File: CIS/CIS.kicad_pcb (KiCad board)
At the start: 6 copper layers, 125 x 32.5 mm, 187 parts, among them J1 Conn_01x12, J2 RJ45_Abracon_ARJP11A-MASA-B-A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, J3 SJ1-3533NG, J4 DEBUG TAG, K1 K_9999, P3 K_0023, Q1 Q_0002, Q2 Q_0002, Q3 Q_0002, SW1 SW_0003, SW2 SW_0003, SW3 SW_0003, SW4 SW_0003, SW5 SW_0003, U1 U_0076, U14 U_0101, U16 U_0049, U17 U_0049, U2 STM32H745IIKx, U3 U_0103, U4 U_1001, U5 U_0081, U6 U_0097, U7 PCM5102, U8 ICM-20602

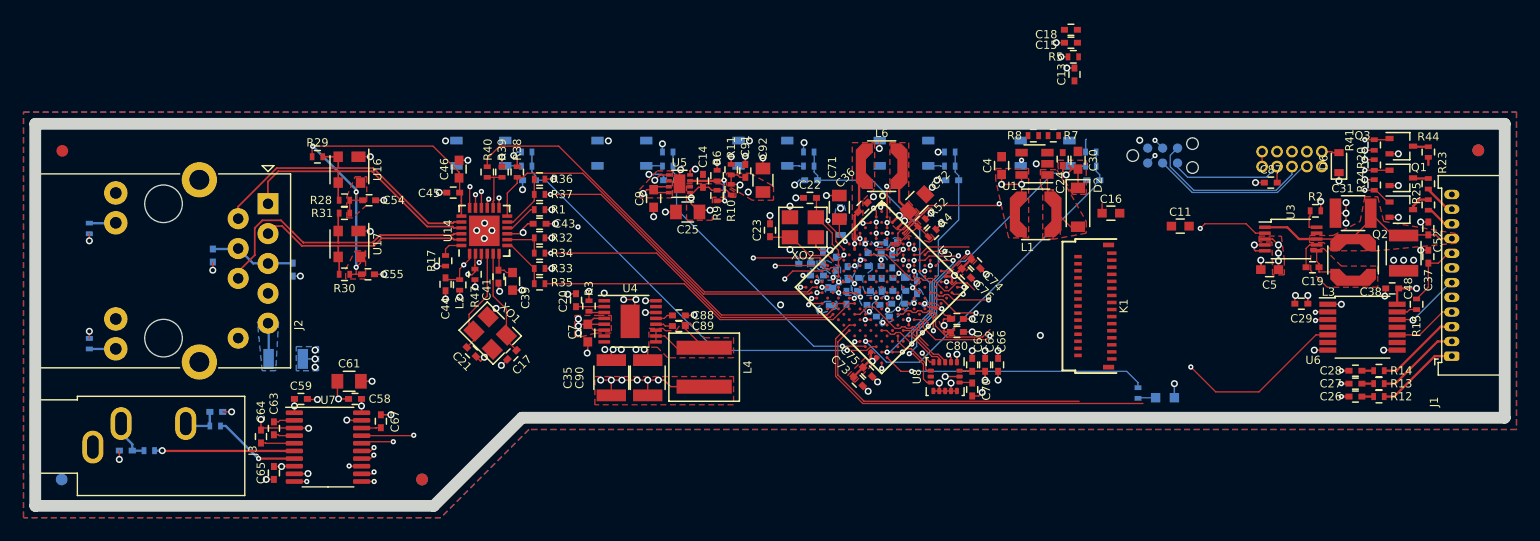
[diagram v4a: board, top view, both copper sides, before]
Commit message: Update oled connector / complete 3D missing part
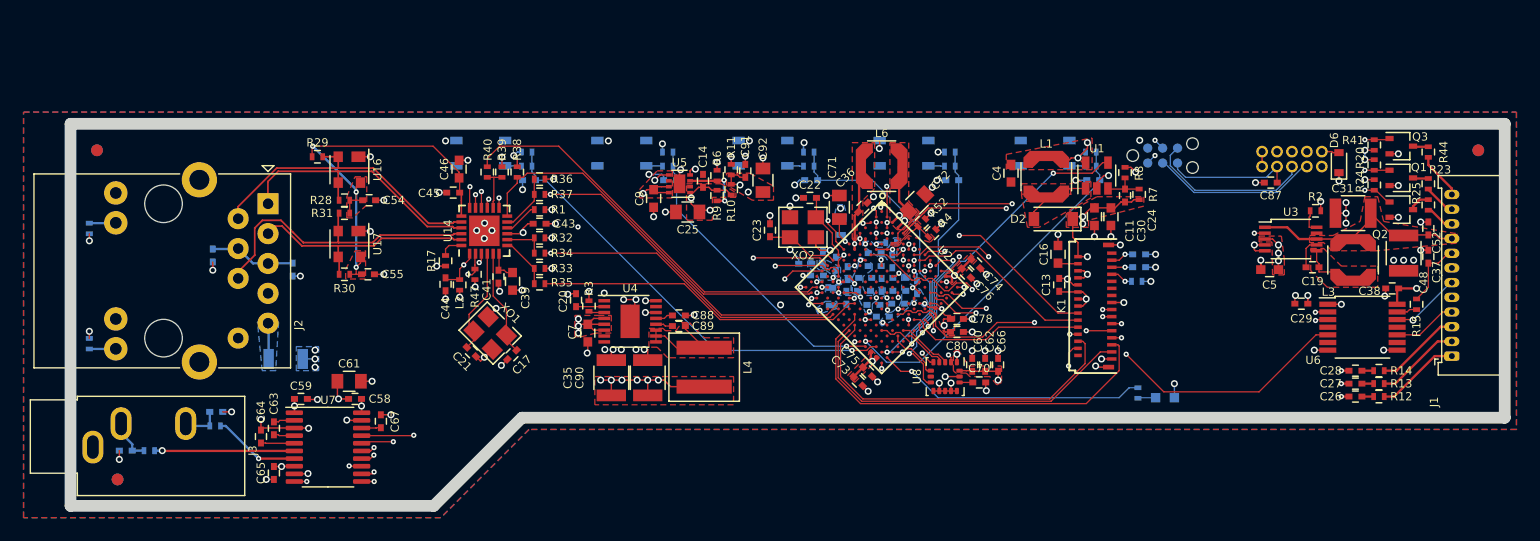
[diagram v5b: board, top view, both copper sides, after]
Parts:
- removed REF4: CircleWhite1mm, DVB_Fiducials:REF_1mm
- added G***: LOGO, DVB_Mechanicals:RESO-NANCE_SSS_LOGO, B.Cu at (50.8, 74.9)
- added G***: LOGO, DVB_Mechanicals:RESO-NANCE_SSS-2_LOGO, B.Cu at (150.2, 84.7)
- added REF12: CircleWhite1mm, DVB_Fiducials:REF_1mm, B.Cu at (46.4, 74.8)
- C15, C18, R5: moved to B.Cu
- moved REF2 25.9 mm to (48.1, 102.8)
- moved C15 20.0 mm to (135.0, 84.7), turned to 0 degrees
- moved C18 20.0 mm to (135.0, 83.6), turned to 0 degrees
- moved R5 19.8 mm to (134.8, 85.9), turned to 180 degrees
- moved C13 17.9 mm to (128.2, 86.2)
- moved R7 8.85 mm to (135.0, 78.5), turned to 90 degrees
- moved R8 8.41 mm to (133.8, 76.7), turned to 90 degrees
- moved C11 7.34 mm to (131.2, 80.4), turned to 270 degrees
- moved C24 6.14 mm to (133.8, 78.6)
- moved C16 5.70 mm to (128.1, 83.6), turned to 90 degrees
- moved C30 5.56 mm to (132.6, 80.4), turned to 270 degrees
- moved U1 5.39 mm to (131.4, 76.9), turned to 90 degrees
- moved REF11 4.75 mm to (48.1, 102.8)
- moved L1 3.32 mm to (127.1, 77.0), turned to 270 degrees
- moved REF1 2.95 mm to (46.4, 74.8)
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- renumbered REF2 to REF1, REF4 to REF11, REF3 to REF13, REF1 to REF3
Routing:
- net /FMC_D5: track 8.34 -> 35.1 mm
- net /DEBUG_RX: track 28.8 -> 51.8 mm
- net /FMC_NEx: track 4.95 -> 19.3 mm, vias 0 -> 2
- net /FMC_Ax: track 10.9 -> 23.5 mm, vias 0 -> 2
- net /FMC_D1: track 9.95 -> 20.8 mm, vias 0 -> 2
- net GND: track 111.1 -> 121.2 mm, vias 133 -> 140
- net /FMC_D2: track 25.3 -> 15.7 mm, vias 1 -> 2
- net /DEBUG_TX: track 44.6 -> 53.4 mm, vias 0 -> 1
- net /FMC_NWE: track 24.7 -> 16.3 mm, vias 1 -> 0
- net /FMC_D0: track 23.0 -> 15.3 mm, vias 1 -> 0
- net /OLED_RESET: track 30.7 -> 23.4 mm, vias 1 -> 2
- net /FMC_D6: track 28.4 -> 21.6 mm, vias 1 -> 2
- net /SWD-IO: track 31.5 -> 37.9 mm, vias 3 -> 2
- net +3.3V: track 66.0 -> 71.3 mm, vias 49 -> 50
- net /12V_EN: track 19.8 -> 24.5 mm, vias 1 -> 2
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- added copper zone on POWER.Cu, net +12V
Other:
- board size 125 x 32.5 mm -> 122 x 32.5 mm

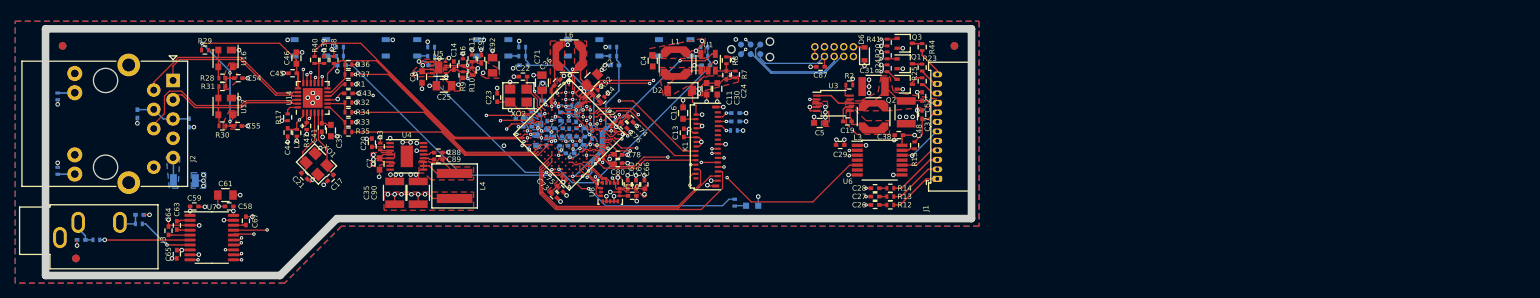
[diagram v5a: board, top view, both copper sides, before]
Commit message: Incert CIS connector
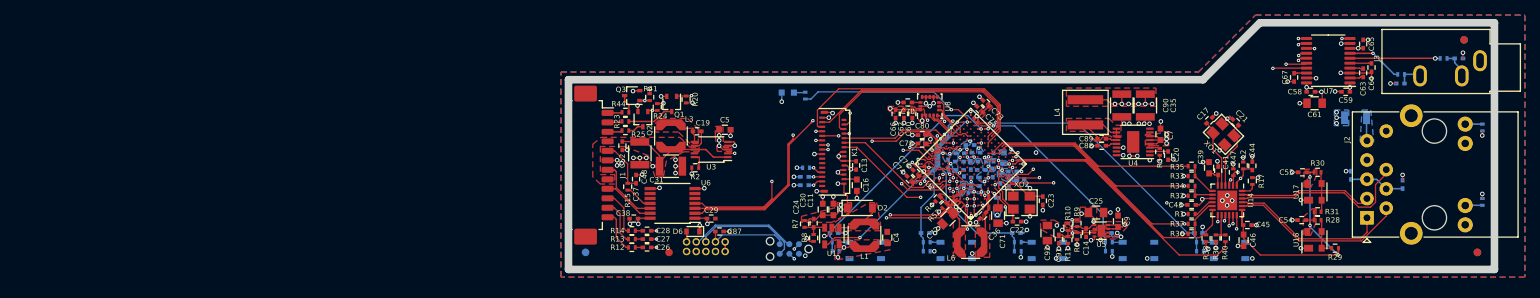
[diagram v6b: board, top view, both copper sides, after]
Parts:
- J1: value Conn_01x12 -> K_9998; footprint DVB_Connectors:Molex_PicoBlade_53048-1210_1x12_P1.25mm_Horizontal -> DVB_Connectors:Molex_PicoBlade_53261-1271_1x12-1MP_P1.25mm_Horizontal
- moved J3 188.5 mm to (233.1, 76.7), turned to 270 degrees
- moved REF1 188.4 mm to (232.8, 102.0), turned to 90 degrees
- moved REF12 188.4 mm to (232.8, 102.0), turned to 180 degrees
- moved R48 188.2 mm to (233.4, 95.3), turned to 90 degrees
- moved R49 187.8 mm to (233.4, 85.5), turned to 270 degrees
- moved REF11 185.2 mm to (231.0, 74.0), turned to 180 degrees
- moved REF2 185.2 mm to (231.0, 74.0), turned to 90 degrees
- moved C69 183.1 mm to (230.3, 76.4), turned to 0 degrees
- moved R50 179.1 mm to (228.3, 76.4), turned to 0 degrees
- moved G*** 172.8 mm to (223.6, 74.1), turned to 180 degrees
- moved R51 167.5 mm to (222.7, 78.5), turned to 180 degrees
- moved C68 167.0 mm to (222.6, 79.7), turned to 180 degrees
- moved C49 167.0 mm to (222.9, 93.0), turned to 90 degrees
- moved C64 160.0 mm to (218.8, 77.6), turned to 90 degrees
- moved C65 158.7 mm to (217.7, 74.5), turned to 90 degrees
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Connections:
- J1 pad 1: Net-(J1-Pad1) -> /CIS_VLED_B
- J1 pad 10: /CIS_VLED_G -> Net-(J1-Pad10)
- J1 pad 11: /CIS_VLED_R -> Net-(J1-Pad11)
- J1 pad 12: /CIS_VLED_B -> Net-(J1-Pad12)
- J1 pad 2: Net-(J1-Pad2) -> /CIS_VLED_R
- J1 pad 3: Net-(J1-Pad3) -> /CIS_VLED_G
- J1 pad 4: /CIS_RS_TTL -> +5V
- J1 pad 5: +5V -> Net-(C37-Pad2)
- J1 pad 6: /CIS_SP_TTL -> GND
- J1 pad 7: GND -> /CIS_SP_TTL
- J1 pad 8: Net-(C37-Pad2) -> +5V
- J1 pad 9: +5V -> /CIS_RS_TTL
- K1 pad 30: (no net) -> Net-(K1-Pad30)
- K1 pad 9: (no net) -> Net-(K1-Pad9)
- P3 pad 7: (no net) -> Net-(P3-Pad7)
- R12 pad 2: Net-(J1-Pad1) -> Net-(J1-Pad12)
- R13 pad 2: Net-(J1-Pad2) -> Net-(J1-Pad11)
- R14 pad 2: Net-(J1-Pad3) -> Net-(J1-Pad10)
- SW1 pad 1: (no net) -> Net-(SW1-Pad1)
- SW1 pad 4: (no net) -> Net-(SW1-Pad4)
- SW2 pad 1: (no net) -> Net-(SW2-Pad1)
- SW2 pad 4: (no net) -> Net-(SW2-Pad4)
- SW3 pad 1: (no net) -> Net-(SW3-Pad1)
- SW3 pad 4: (no net) -> Net-(SW3-Pad4)
- SW4 pad 1: (no net) -> Net-(SW4-Pad1)
- SW4 pad 4: (no net) -> Net-(SW4-Pad4)
- SW5 pad 1: (no net) -> Net-(SW5-Pad1)
- SW5 pad 4: (no net) -> Net-(SW5-Pad4)
- U2 pad A6: (no net) -> Net-(U2-PadA6)
- U2 pad A8: (no net) -> Net-(U2-PadA8)
- U2 pad B10: (no net) -> Net-(U2-PadB10)
- U2 pad B11: (no net) -> Net-(U2-PadB11)
- U2 pad B12: (no net) -> Net-(U2-PadB12)
- U2 pad B14: (no net) -> Net-(U2-PadB14)
- U2 pad B2: (no net) -> Net-(U2-PadB2)
- U2 pad B4: (no net) -> Net-(U2-PadB4)
- U2 pad B6: (no net) -> Net-(U2-PadB6)
- U2 pad C11: (no net) -> Net-(U2-PadC11)
- U2 pad C12: (no net) -> Net-(U2-PadC12)
- U2 pad C13: (no net) -> Net-(U2-PadC13)
- U2 pad C14: (no net) -> Net-(U2-PadC14)
- U2 pad C15: (no net) -> Net-(U2-PadC15)
- U2 pad C4: (no net) -> Net-(U2-PadC4)
- U2 pad C6: (no net) -> Net-(U2-PadC6)
- U2 pad C8: (no net) -> Net-(U2-PadC8)
- U2 pad D1: (no net) -> Net-(U2-PadD1)
- U2 pad D12: (no net) -> Net-(U2-PadD12)
- U2 pad D15: (no net) -> Net-(U2-PadD15)
- U2 pad D2: (no net) -> Net-(U2-PadD2)
- U2 pad D7: (no net) -> Net-(U2-PadD7)
- U2 pad D8: (no net) -> Net-(U2-PadD8)
- U2 pad E13: (no net) -> Net-(U2-PadE13)
- U2 pad E14: /CIS_LED_R -> /CIS_LED_B
- U2 pad E3: (no net) -> Net-(U2-PadE3)
- U2 pad F14: (no net) -> Net-(U2-PadF14)
- U2 pad F3: (no net) -> Net-(U2-PadF3)
- U2 pad G12: (no net) -> Net-(U2-PadG12)
- U2 pad G13: (no net) -> Net-(U2-PadG13)
- U2 pad G14: (no net) -> Net-(U2-PadG14)
- U2 pad G3: (no net) -> Net-(U2-PadG3)
- U2 pad H13: (no net) -> Net-(U2-PadH13)
- U2 pad H15: /CIS_LED_G -> /CIS_LED_R
- U2 pad H2: (no net) -> Net-(U2-PadH2)
- U2 pad H3: (no net) -> Net-(U2-PadH3)
- U2 pad H4: (no net) -> Net-(U2-PadH4)
- U2 pad J13: (no net) -> Net-(U2-PadJ13)
- U2 pad J15: (no net) -> Net-(U2-PadJ15)
- U2 pad J2: (no net) -> Net-(U2-PadJ2)
- U2 pad J3: (no net) -> Net-(U2-PadJ3)
- U2 pad J4: (no net) -> Net-(U2-PadJ4)
- U2 pad K13: (no net) -> Net-(U2-PadK13)
- U2 pad K3: (no net) -> Net-(U2-PadK3)
- U2 pad L13: (no net) -> Net-(U2-PadL13)
- U2 pad L15: (no net) -> Net-(U2-PadL15)
- U2 pad L2: (no net) -> Net-(U2-PadL2)
- U2 pad M11: (no net) -> Net-(U2-PadM11)
- U2 pad M13: (no net) -> Net-(U2-PadM13)
- U2 pad M14: (no net) -> Net-(U2-PadM14)
- U2 pad M15: (no net) -> Net-(U2-PadM15)
- U2 pad M2: (no net) -> Net-(U2-PadM2)
- U2 pad M8: (no net) -> Net-(U2-PadM8)
- U2 pad N1: (no net) -> Net-(U2-PadN1)
- U2 pad N10: (no net) -> Net-(U2-PadN10)
- U2 pad N11: (no net) -> Net-(U2-PadN11)
- U2 pad N12: (no net) -> Net-(U2-PadN12)
- U2 pad N13: (no net) -> Net-(U2-PadN13)
- U2 pad N14: (no net) -> Net-(U2-PadN14)
- U2 pad N15: /CIS_LED_B -> /CIS_LED_G
- U2 pad N4: (no net) -> Net-(U2-PadN4)
- U2 pad N5: (no net) -> Net-(U2-PadN5)
- U2 pad N7: (no net) -> Net-(U2-PadN7)
- U2 pad N9: (no net) -> Net-(U2-PadN9)
- U2 pad P1: (no net) -> Net-(U2-PadP1)
- U2 pad P10: (no net) -> Net-(U2-PadP10)
- U2 pad P11: (no net) -> Net-(U2-PadP11)
- U2 pad P4: (no net) -> Net-(U2-PadP4)
- U2 pad P5: (no net) -> Net-(U2-PadP5)
- U2 pad P6: (no net) -> Net-(U2-PadP6)
- U2 pad P7: (no net) -> Net-(U2-PadP7)
- U2 pad P8: (no net) -> Net-(U2-PadP8)
- U2 pad R10: (no net) -> Net-(U2-PadR10)
- U2 pad R5: (no net) -> Net-(U2-PadR5)
- U2 pad R7: (no net) -> Net-(U2-PadR7)
- U2 pad R8: (no net) -> Net-(U2-PadR8)
- U3 pad 9: (no net) -> Net-(U3-Pad9)
- U4 pad 15: (no net) -> Net-(U4-Pad15)
- U4 pad 7: (no net) -> Net-(U4-Pad7)
- U5 pad 6: (no net) -> Net-(U5-Pad6)
- U6 pad 10: /CIS_RS_TTL -> Net-(U6-Pad10)
- U6 pad 11: (no net) -> /CIS_CP_TTL
- U6 pad 13: /CIS_CP_TTL -> /CIS_RS_TTL
- U6 pad 2: /CIS_CP -> /CIS_RS
- U6 pad 4: (no net) -> /CIS_CP
- U6 pad 5: /CIS_RS -> Net-(U6-Pad5)
- U6 pad 6: (no net) -> Net-(U6-Pad6)
- U6 pad 9: (no net) -> Net-(U6-Pad9)
- U8 pad 7: (no net) -> Net-(U8-Pad7)
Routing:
- net /CIS_ADC_3: track 50.1 -> 68.1 mm
- net /CIS_ADC_2: track 51.8 -> 67.6 mm
- net /CIS_ADC_1: track 54.5 -> 68.2 mm
- net Net-(J1-Pad3): track 7.30 -> 0.00 mm
- net Net-(J1-Pad2): track 7.24 -> 0.00 mm
- net Net-(J1-Pad1): track 7.18 -> 0.00 mm
- net Net-(J1-Pad10): track 0.00 -> 6.10 mm
- net Net-(J1-Pad11): track 0.00 -> 5.95 mm
- net Net-(J1-Pad12): track 0.00 -> 5.80 mm
- net /CIS_LED_R: track 44.1 -> 38.4 mm
- net +15: track 114.1 -> 108.9 mm
- net Net-(Q1-Pad3): track 1.32 -> 6.19 mm
- net /5V_EN: track 33.3 -> 37.6 mm
- net GND: track 121.2 -> 125.4 mm, vias 140 -> 142
- net /CIS_RS: track 37.5 -> 40.8 mm
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- removed copper zone on POWER.Cu, net +5V
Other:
- outline, holes or cut-outs redrawn
- board text added: "01/2021 v1.0.0"
- board text removed: "2020 - v1.0.0"
